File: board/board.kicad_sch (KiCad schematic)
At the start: 4 parts, among them J1 012_CAN, J2 Conn_01x03_Male

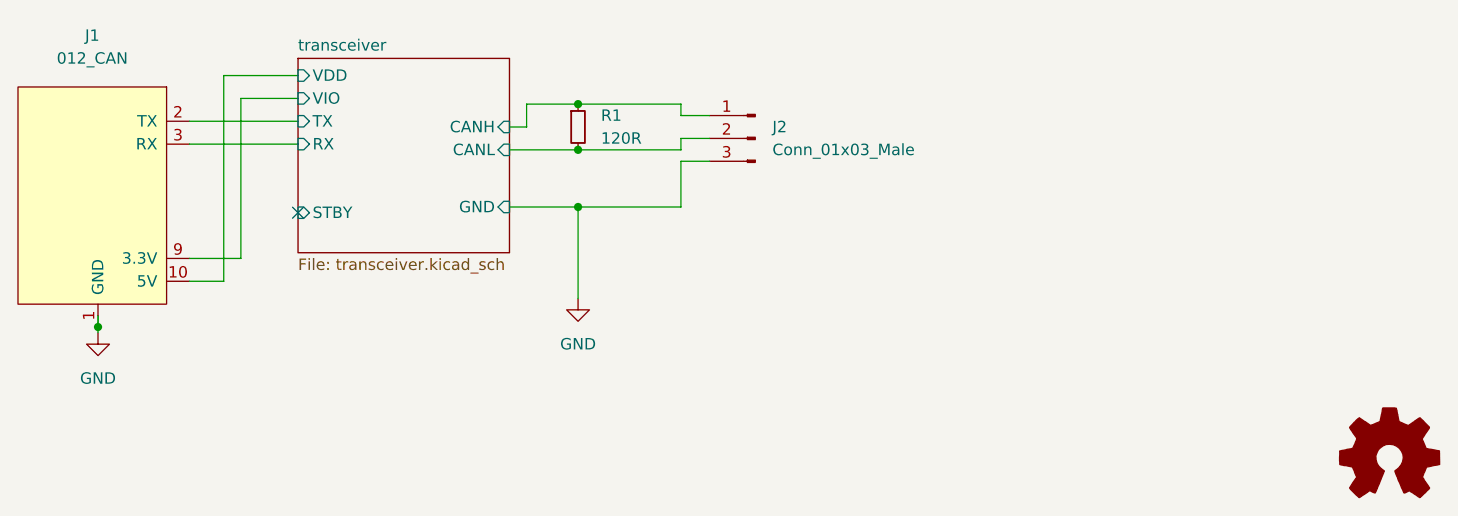
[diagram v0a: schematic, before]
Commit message: changed transceiver chip to be more availible TJA1044GT version
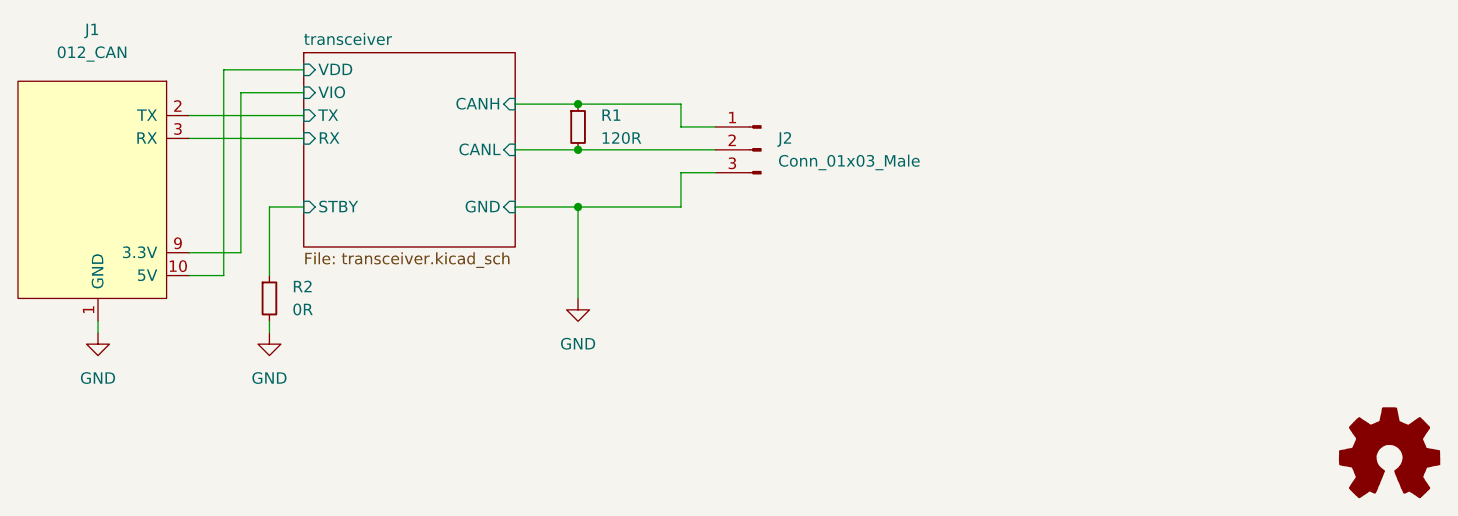
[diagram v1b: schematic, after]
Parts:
- added R2: 0R, Resistor_SMD:R_0603_1608Metric, symbol Device:R_Small
- R1: lcsc (none) -> C17437
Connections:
- net GND: now also R2.2
- net transceiver/STBY: now also R2.1
- no-connect marks 1 -> 0
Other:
- moved on the sheet: J1, J2
